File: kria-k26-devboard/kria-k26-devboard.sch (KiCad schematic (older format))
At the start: 1 part

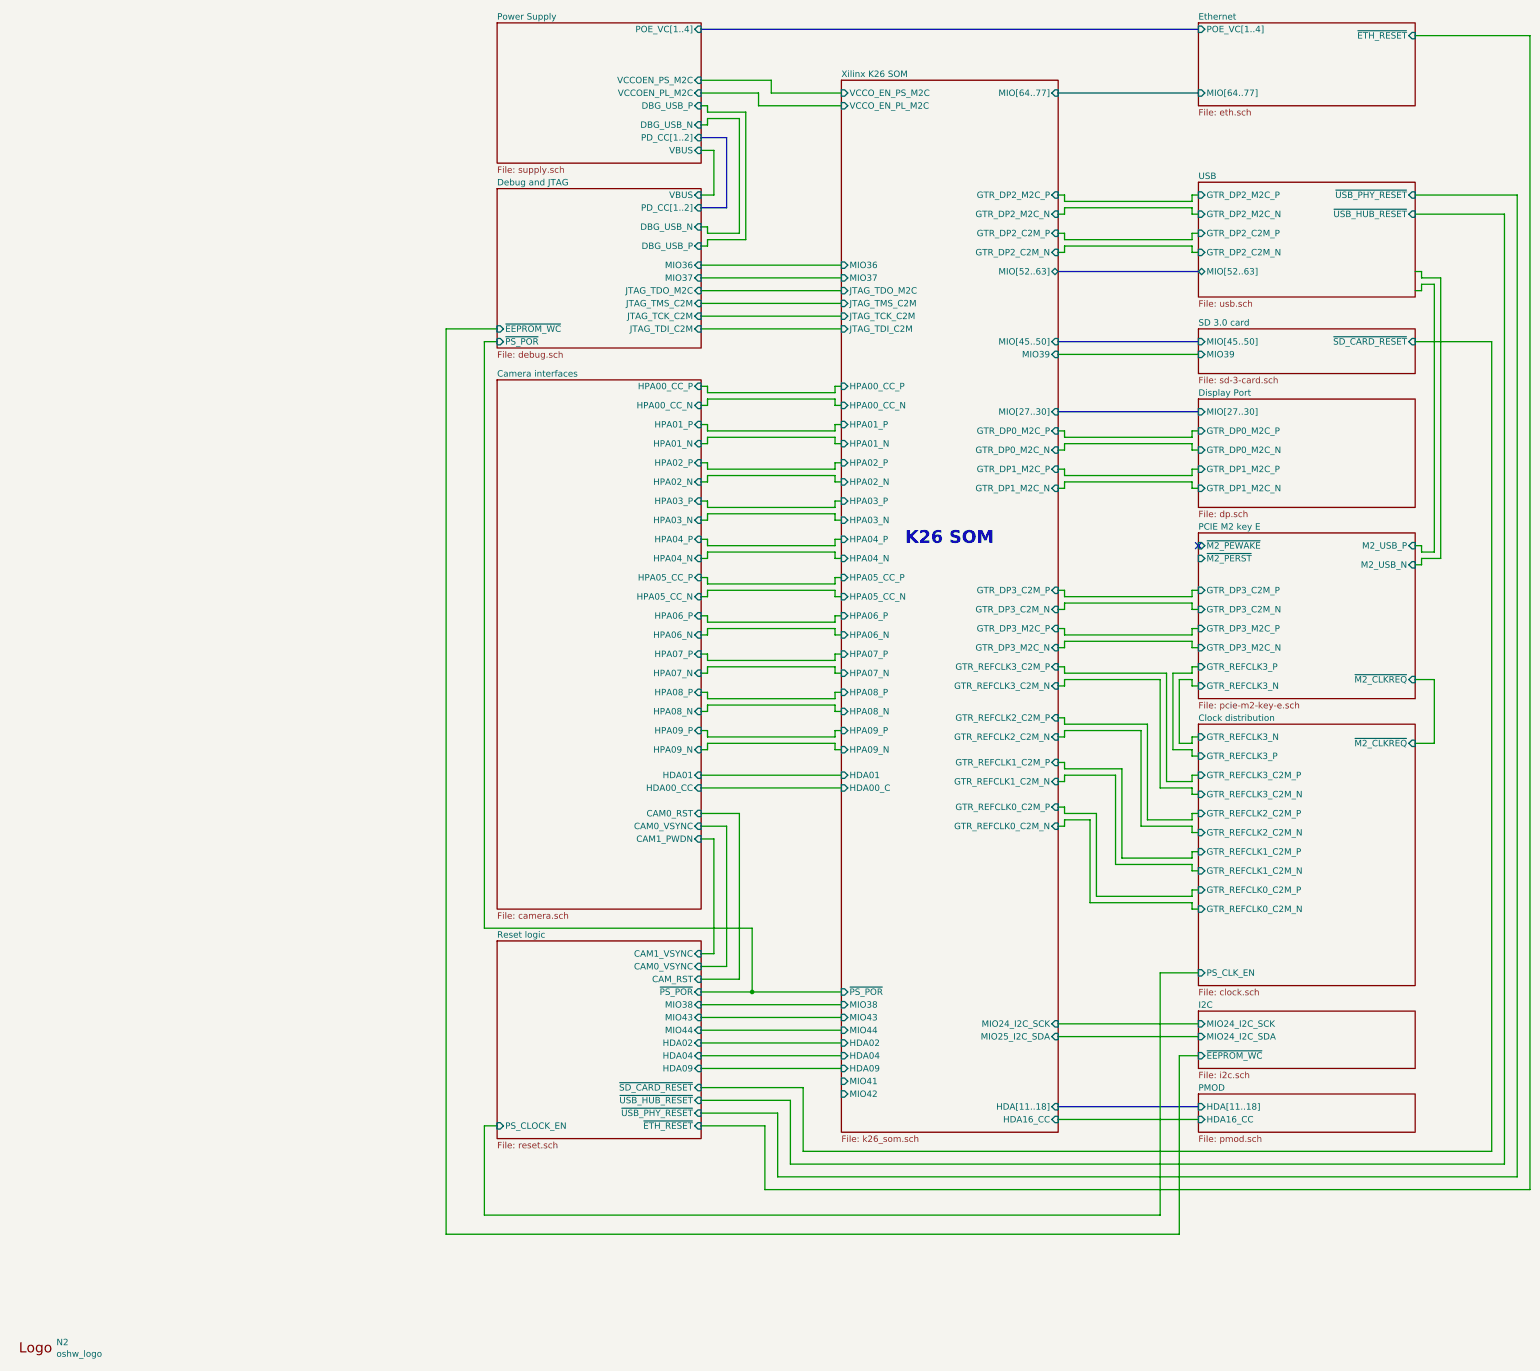
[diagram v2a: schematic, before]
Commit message: Finished tidying up the schematic
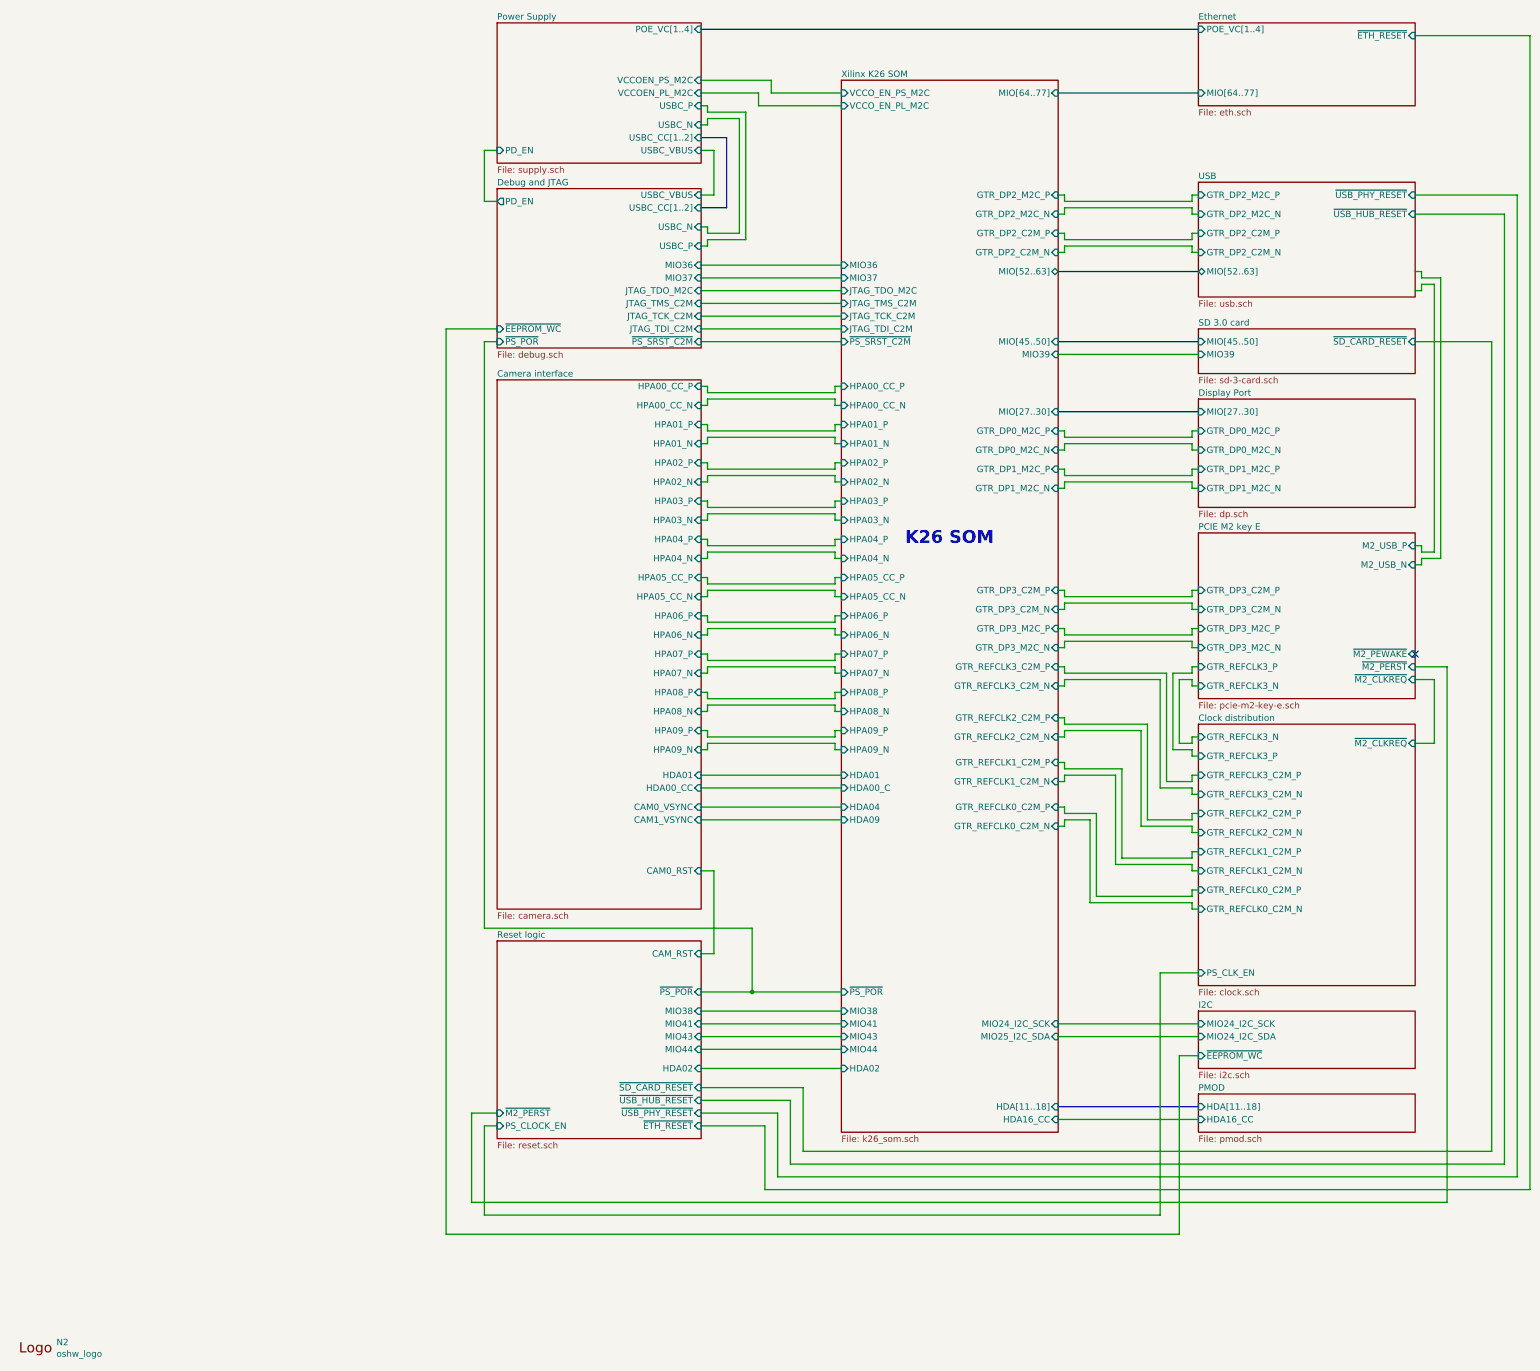
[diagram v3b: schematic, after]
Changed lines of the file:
@@
 Comment4 ""
 $EndDescr
-$Sheet
-S 4350 650  1600 1100
-U 63C44BC2
-F0 "Power Supply" 50
-F1 "supply.sch" 50
-F2 "PD_CC[1..2]" I R 5950 1550 50
-F3 "VCCOEN_PS_M2C" I R 5950 1100 50
-F4 "VCCOEN_PL_M2C" I R 5950 1200 50
-F5 "POE_VC[1..4]" I R 5950 700 50
-F6 "DBG_USB_P" I R 5950 1300 50
-F7 "DBG_USB_N" I R 5950 1450 50
-F8 "VBUS" I R 5950 1650 50
-$EndSheet
-$Sheet
-S 4350 1950 1600 1250
-U 625B0244
-F0 "Debug and JTAG" 50
-F1 "debug.sch" 50
-F2 "PD_CC[1..2]" I R 5950 2100 50
-F3 "JTAG_TDO_M2C" I R 5950 2750 50
-F4 "JTAG_TMS_C2M" I R 5950 2850 50
-F5 "JTAG_TCK_C2M" I R 5950 2950 50
-F6 "JTAG_TDI_C2M" I R 5950 3050 50
-F7 "DBG_USB_P" I R 5950 2400 50
-F8 "DBG_USB_N" I R 5950 2250 50
-F9 "MIO37" I R 5950 2650 50
-F10 "MIO36" I R 5950 2550 50
-F11 "VBUS" I R 5950 2000 50
-F12 "~PS_POR" I L 4350 3150 50
-F13 "~EEPROM_WC" I L 4350 3050 50
-$EndSheet
 Wire Wire Line
 	5950 1200 6400 1200
@@
 F9 "M2_USB_N" I R 11550 4900 50
 F10 "~M2_CLKREQ" I R 11550 5800 50
-F11 "~M2_PEWAKE" I L 9850 4750 50
-F12 "~M2_PERST" I L 9850 4850 50
+F11 "~M2_PEWAKE" I R 11550 5600 50
+F12 "~M2_PERST" I R 11550 5700 50
 $EndSheet
 Wire Wire Line
@@
 	12450 750  11550 750
 Wire Wire Line
-	5950 2250 6000 2250
-Wire Wire Line
-	6000 2250 6000 2300
-Wire Wire Line
-	6000 2300 6250 2300
-Wire Wire Line
 	6500 1200 7050 1200
 Wire Wire Line
 	6400 1300 7050 1300
-Wire Wire Line
-	6300 2350 6000 2350
-Wire Wire Line
-	6000 2350 6000 2400
-Wire Wire Line
-	6000 2400 5950 2400
 $Sheet
 S 4350 3450 1600 4150
 U 63CB76CF
-F0 "Camera interfaces" 50
+F0 "Camera interface" 50
 F1 "camera.sch" 50
 F2 "HPA00_CC_P" I R 5950 3500 50
@@
 F22 "HDA01" I R 5950 6550 50
 F23 "HDA00_CC" I R 5950 6650 50
-F24 "CAM0_RST" I R 5950 6850 50
-F25 "CAM0_VSYNC" I R 5950 6950 50
-F26 "CAM1_PWDN" I R 5950 7050 50
+F24 "CAM0_VSYNC" I R 5950 6800 50
+F25 "CAM1_VSYNC" I R 5950 6900 50
+F26 "CAM0_RST" I R 5950 7300 50
 $EndSheet
 Wire Wire Line
@@
 	7050 6650 5950 6650
 Wire Wire Line
-	5950 7950 6050 7950
-Wire Wire Line
-	6050 7950 6050 7050
-Wire Wire Line
-	6050 7050 5950 7050
-Wire Wire Line
-	5950 8050 6150 8050
-Wire Wire Line
-	6150 8050 6150 6950
-Wire Wire Line
-	6150 6950 5950 6950
-Wire Wire Line
-	5950 8150 6250 8150
-Wire Wire Line
-	6250 8150 6250 6850
-Wire Wire Line
-	6250 6850 5950 6850
-Wire Wire Line
-	5950 8350 7050 8350
-Wire Wire Line
-	7050 8450 5950 8450
-Wire Wire Line
-	5950 8550 7050 8550
-Wire Wire Line
-	7050 8650 5950 8650
-Wire Wire Line
-	5950 8750 7050 8750
-Wire Wire Line
-	7050 8850 5950 8850
+	5950 8400 7050 8400
+Wire Wire Line
+	7050 8500 5950 8500
+Wire Wire Line
+	5950 8600 7050 8600
+Wire Wire Line
+	7050 8700 5950 8700
 Wire Wire Line
 	5950 9000 6750 9000
@@
 Wire Wire Line
 	6350 8250 7050 8250
-Wire Wire Line
-	6000 1300 6000 1350
-Wire Wire Line
-	5950 1300 6000 1300
-Wire Wire Line
-	6000 1450 5950 1450
-Wire Wire Line
-	6000 1400 6000 1450
-Wire Wire Line
-	6250 1400 6000 1400
-Wire Wire Line
-	6250 1400 6250 2300
-Wire Wire Line
-	6300 1350 6300 2350
-Wire Wire Line
-	6000 1350 6300 1350
 Wire Wire Line
 	6400 1200 6400 1300
@@
 F43 "HDA00_C" I L 7050 6650 50
 F44 "HDA01" I L 7050 6550 50
-F45 "MIO38" I L 7050 8350 50
-F46 "MIO44" I L 7050 8550 50
-F47 "MIO43" I L 7050 8450 50
-F48 "HDA04" I L 7050 8750 50
-F49 "HDA02" I L 7050 8650 50
-F50 "HDA09" I L 7050 8850 50
+F45 "MIO38" I L 7050 8400 50
+F46 "MIO44" I L 7050 8700 50
+F47 "MIO43" I L 7050 8600 50
+F48 "HDA04" I L 7050 6800 50
+F49 "HDA02" I L 7050 8850 50
+F50 "HDA09" I L 7050 6900 50
 F51 "MIO36" I L 7050 2550 50
 F52 "MIO37" I L 7050 2650 50
@@
 F66 "GTR_REFCLK0_C2M_P" I R 8750 6800 50
 F67 "GTR_REFCLK0_C2M_N" I R 8750 6950 50
-F68 "MIO41" I L 7050 8950 50
-F69 "MIO42" I L 7050 9050 50
+F68 "MIO41" I L 7050 8500 50
+F69 "~PS_SRST_C2M" I L 7050 3150 50
 $EndSheet
 Wire Wire Line
@@
 Wire Wire Line
 	11700 6300 11550 6300
-NoConn ~ 9850 4750
+NoConn ~ 11550 5600
 $Sheet
 S 4350 7850 1600 1550
@@
 F0 "Reset logic" 50
 F1 "reset.sch" 50
-F2 "MIO43" I R 5950 8450 50
-F3 "MIO44" I R 5950 8550 50
-F4 "MIO38" I R 5950 8350 50
-F5 "HDA02" I R 5950 8650 50
-F6 "HDA04" I R 5950 8750 50
-F7 "HDA09" I R 5950 8850 50
-F8 "~PS_POR" I R 5950 8250 50
-F9 "~USB_PHY_RESET" I R 5950 9200 50
-F10 "~USB_HUB_RESET" I R 5950 9100 50
-F11 "~ETH_RESET" I R 5950 9300 50
-F12 "~SD_CARD_RESET" I R 5950 9000 50
-F13 "PS_CLOCK_EN" I L 4350 9300 50
-F14 "CAM_RST" I R 5950 8150 50
-F15 "CAM0_VSYNC" I R 5950 8050 50
-F16 "CAM1_VSYNC" I R 5950 7950 50
-$EndSheet
+F2 "MIO43" I R 5950 8600 50
+F3 "MIO44" I R 5950 8700 50
+F4 "MIO38" I R 5950 8400 50
+F5 "HDA02" I R 5950 8850 50
+F6 "~PS_POR" I R 5950 8250 50
+F7 "~USB_PHY_RESET" I R 5950 9200 50
+F8 "~USB_HUB_RESET" I R 5950 9100 50
+F9 "~ETH_RESET" I R 5950 9300 50
+F10 "~SD_CARD_RESET" I R 5950 9000 50
+F11 "PS_CLOCK_EN" I L 4350 9300 50
+F12 "MIO41" I R 5950 8500 50
+F13 "~M2_PERST" I L 4350 9200 50
+F14 "CAM_RST" I R 5950 7950 50
+$EndSheet
+$Sheet
+S 4350 1950 1600 1250
+U 625B0244
+F0 "Debug and JTAG" 50
+F1 "debug.sch" 50
+F2 "JTAG_TDO_M2C" I R 5950 2750 50
+F3 "JTAG_TMS_C2M" I R 5950 2850 50
+F4 "JTAG_TCK_C2M" I R 5950 2950 50
+F5 "JTAG_TDI_C2M" I R 5950 3050 50
+F6 "MIO37" I R 5950 2650 50
+F7 "MIO36" I R 5950 2550 50
+F8 "~PS_POR" I L 4350 3150 50
+F9 "~EEPROM_WC" I L 4350 3050 50
+F10 "USBC_CC[1..2]" I R 5950 2100 50
+F11 "USBC_VBUS" I R 5950 2000 50
+F12 "USBC_P" I R 5950 2400 50
+F13 "USBC_N" I R 5950 2250 50
+F14 "PD_EN" O L 4350 2050 50
+F15 "~PS_SRST_C2M" I R 5950 3150 50
+$EndSheet
+$Sheet
+S 4350 650  1600 1100
+U 63C44BC2
+F0 "Power Supply" 50
+F1 "supply.sch" 50
+F2 "VCCOEN_PS_M2C" I R 5950 1100 50
+F3 "VCCOEN_PL_M2C" I R 5950 1200 50
+F4 "POE_VC[1..4]" I R 5950 700 50
+F5 "USBC_CC[1..2]" I R 5950 1550 50
+F6 "USBC_P" I R 5950 1300 50
+F7 "USBC_N" I R 5950 1450 50
+F8 "USBC_VBUS" I R 5950 1650 50
+F9 "PD_EN" I L 4350 1650 50
+$EndSheet
+Wire Wire Line
+	6000 2400 5950 2400
+Wire Wire Line
+	6000 2350 6000 2400
+Wire Wire Line
+	6300 2350 6000 2350
+Wire Wire Line
+	6000 2300 6250 2300
+Wire Wire Line
+	6000 2250 6000 2300
+Wire Wire Line
+	5950 2250 6000 2250
+Wire Wire Line
+	6000 1300 6000 1350
+Wire Wire Line
+	6000 1400 6000 1450
+Wire Wire Line
+	6250 1400 6000 1400
+Wire Wire Line
+	6250 1400 6250 2300
+Wire Wire Line
+	6300 1350 6300 2350
+Wire Wire Line
+	6000 1450 5950 1450
+Wire Wire Line
+	6000 1350 6300 1350
+Wire Wire Line
+	5950 1300 6000 1300
+Wire Wire Line
+	4350 1650 4250 1650
+Wire Wire Line
+	4250 1650 4250 2050
+Wire Wire Line
+	4250 2050 4350 2050
+Wire Wire Line
+	5950 3150 7050 3150
+Wire Wire Line
+	5950 7950 6050 7950
+Wire Wire Line
+	6050 7950 6050 7300
+Wire Wire Line
+	6050 7300 5950 7300
+Wire Wire Line
+	5950 6800 7050 6800
+Wire Wire Line
+	7050 6900 5950 6900
+Wire Wire Line
+	5950 8850 7050 8850
+Wire Wire Line
+	11550 5700 11800 5700
+Wire Wire Line
+	11800 5700 11800 9900
+Wire Wire Line
+	11800 9900 4150 9900
+Wire Wire Line
+	4150 9900 4150 9200
+Wire Wire Line
+	4150 9200 4350 9200
 $EndSCHEMATC

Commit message: Progress in PCB placement
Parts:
- added N2: antmicro_logo, antmicro-footprints:antmicro-logo_scaled_15mm, symbol antmicroMechanicalParts:antmicro_logo
- renumbered N2 to N1
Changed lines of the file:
@@
 F0 "SD 3.0 card" 50
 F1 "sd-3-card.sch" 50
-F2 "MIO[45..50]" I L 9850 3150 50
+F2 "MIO[45..51]" I L 9850 3150 50
 F3 "MIO39" I L 9850 3250 50
 F4 "~SD_CARD_RESET" I R 11550 3150 50
@@
 	9850 8600 8750 8600
 $Comp
-L antmicroMechanicalParts:oshw_logo N2
+L antmicroMechanicalParts:oshw_logo N1
 U 1 1 63FCC534
 P 700 11000
-F 0 "N2" H 894 11003 50  0000 L CNN
+F 0 "N1" H 894 11003 50  0000 L CNN
 F 1 "oshw_logo" H 894 10912 50  0000 L CNN
 F 2 "antmicro-footprints:oshw-logo" H 720 10760 50  0001 C CNN
@@
 F8 "GTR_DP2_M2C_P" I R 8750 2000 50
 F9 "GTR_DP2_M2C_N" I R 8750 2150 50
-F10 "MIO[45..50]" I R 8750 3150 50
+F10 "MIO[45..51]" I R 8750 3150 50
 F11 "MIO39" I R 8750 3250 50
 F12 "MIO[27..30]" I R 8750 3700 50
@@
 Wire Wire Line
 	4150 9200 4350 9200
+$Comp
+L antmicroMechanicalParts:antmicro_logo N2
+U 1 1 6B81F324
+P 650 10850
+F 0 "N2" H 864 10943 50  0000 L CNN
+F 1 "antmicro_logo" H 864 10852 50  0000 L CNN
+F 2 "antmicro-footprints:antmicro-logo_scaled_15mm" H 550 11100 50  0001 C CNN
+F 3 "" H 650 11200 50  0001 C CNN
+	1    650  10850
+	1    0    0    -1
+$EndComp
 $EndSCHEMATC

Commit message: Finished initial component placement
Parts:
- N2: footprint antmicro-footprints:antmicro-logo_scaled_15mm -> antmicro-footprints:antmicro-logo_scaled_30mm
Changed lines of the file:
@@
 F 0 "N2" H 864 10943 50  0000 L CNN
 F 1 "antmicro_logo" H 864 10852 50  0000 L CNN
-F 2 "antmicro-footprints:antmicro-logo_scaled_15mm" H 550 11100 50  0001 C CNN
+F 2 "antmicro-footprints:antmicro-logo_scaled_30mm" H 550 11100 50  0001 C CNN
 F 3 "" H 650 11200 50  0001 C CNN
 	1    650  10850

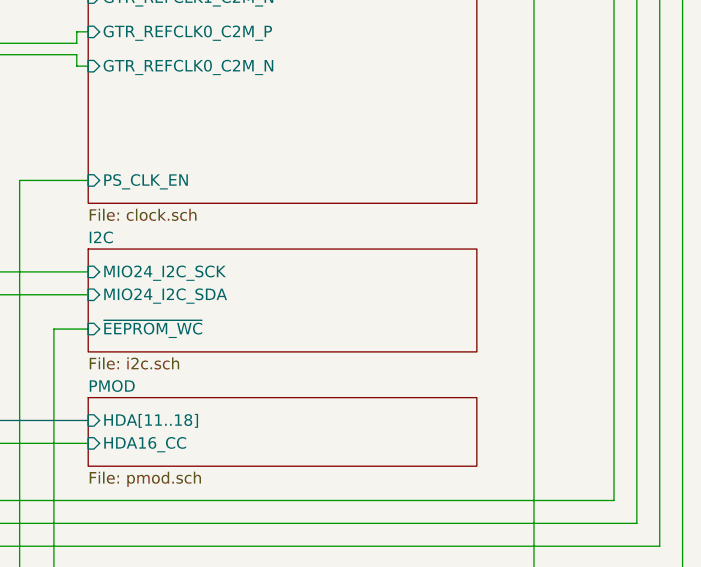
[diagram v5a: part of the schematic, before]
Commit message: Fixed possible FTDI-USB backfeeding issue, finished PS and FTDI power planes creation, finished routing of FTDI/Debug part
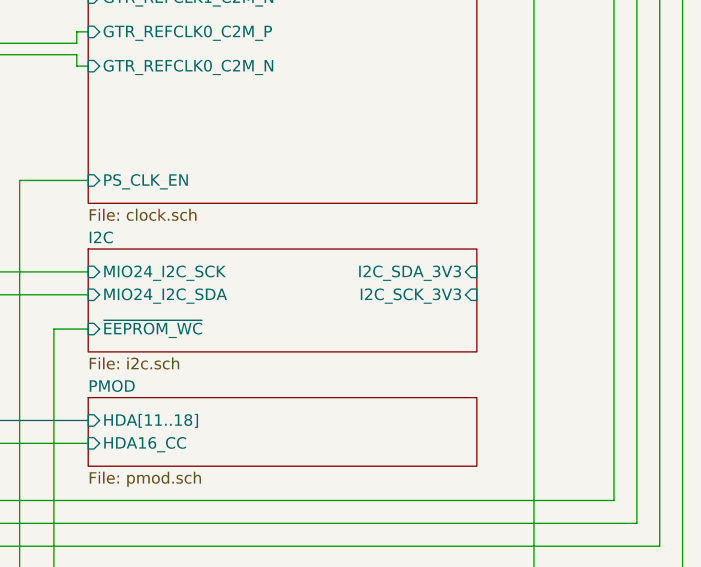
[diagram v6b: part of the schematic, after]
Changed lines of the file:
@@
 F3 "MIO24_I2C_SDA" I L 9850 8600 50
 F4 "~EEPROM_WC" I L 9850 8750 50
+F5 "I2C_SDA_3V3" I R 11550 8500 50
+F6 "I2C_SCK_3V3" I R 11550 8600 50
 $EndSheet
 Wire Wire Line
